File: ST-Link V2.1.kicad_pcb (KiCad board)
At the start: 2 copper layers, 46 parts, among them J1 Conn_01x08, J2 USB_OTG, J4 Conn_01x08, Q1 MMBT3904, U0 stm32, U1 MIC5219-3.3, X1 8MHz

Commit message: duh
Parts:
- C11, C12, C14, C15, C17, C5, C6, C7, C8, R10, R11, R12, R13, R14, R19, R20, R21, R22, R23, R26, R27, R29, R3, R30, R31, R4, R5, R6, R7, R8, R9: moved to F.Cu
- D1, D2, J2, U0: moved to B.Cu
- moved R2 69.0 mm to (126.2, 144.8), turned to 0 degrees
- moved C18 61.8 mm to (126.6, 139.8)
- moved R1 60.9 mm to (131.2, 139.7)
- moved LD2 54.8 mm to (130.2, 129.4)
- moved R9 51.8 mm to (140.9, 134.3)
- moved R10 51.6 mm to (135.6, 139.7)
- moved R11 50.5 mm to (130.6, 144.8)
- moved C11 50.4 mm to (136.9, 124.3)
- moved R14 50.4 mm to (135.0, 144.8)
- moved C14 50.3 mm to (143.5, 124.3)
- moved C12 49.5 mm to (140.2, 124.3), turned to 0 degrees
- moved Q1 48.5 mm to (131.1, 123.6)
- moved C7 46.6 mm to (129.0, 134.3)
- moved C6 45.2 mm to (139.8, 139.8)
- moved R27 41.0 mm to (144.0, 140.0)
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
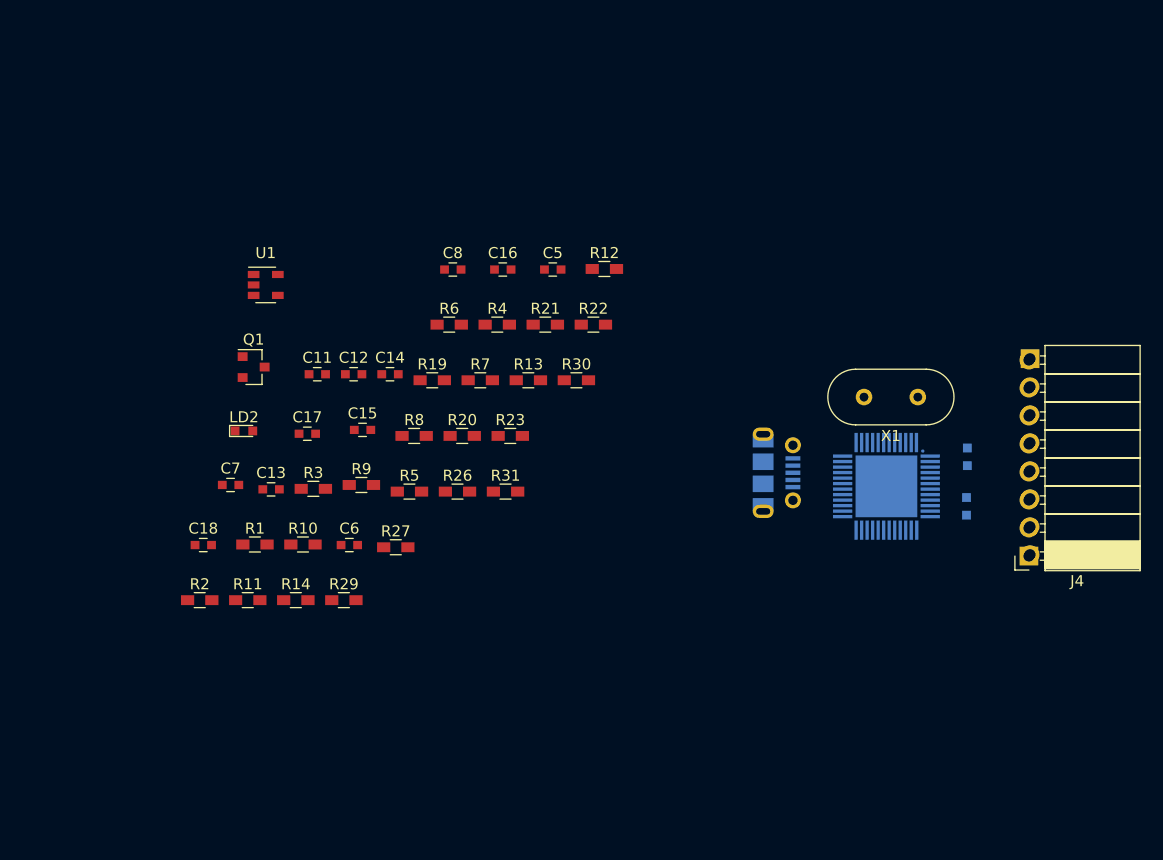
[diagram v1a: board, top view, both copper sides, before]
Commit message: ROUTE RESISTOR
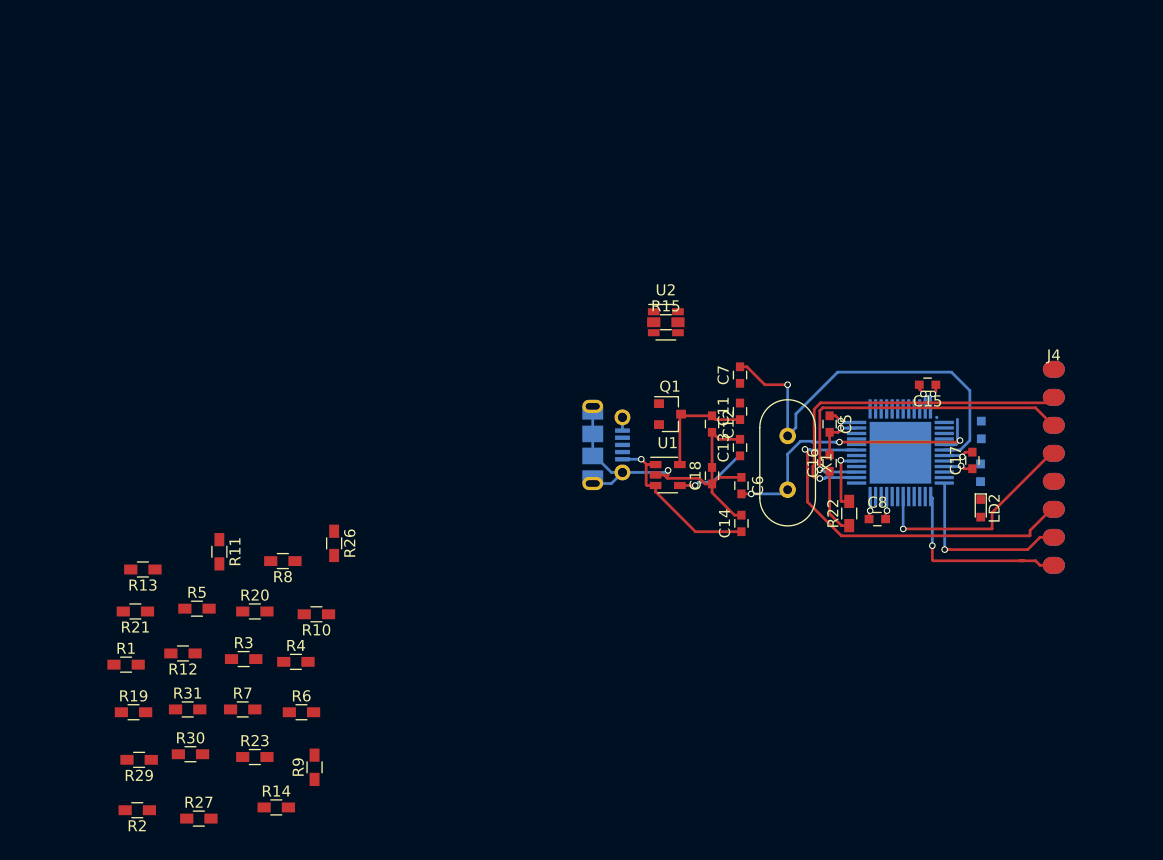
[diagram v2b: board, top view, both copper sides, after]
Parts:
- added R15: 4.7K, Resistors_SMD:R_0603_HandSoldering, F.Cu at (168.5, 119.5)
- added U2: USBLC6-2SC6, TO_SOT_Packages_SMD:SOT-23-6, F.Cu at (168.5, 119.5)
- J1, J4: footprint Socket_Strips:Socket_Strip_Angled_1x08_Pitch2.54mm -> MetalPad:METAL_PAD
- moved LD2 67.2 mm to (197.1, 136.4), turned to 270 degrees
- moved C17 60.4 mm to (196.3, 132.1), turned to 90 degrees
- moved R12 51.8 mm to (124.7, 149.6), turned to 180 degrees
- moved C15 51.4 mm to (192.3, 125.2), turned to 180 degrees
- moved R30 48.8 mm to (125.4, 158.8)
- moved C7 47.3 mm to (175.3, 124.3), turned to 90 degrees
- moved C18 46.6 mm to (172.7, 133.5), turned to 90 degrees
- moved R21 45.4 mm to (120.4, 145.8), turned to 180 degrees
- moved C8 44.7 mm to (187.7, 137.4)
- moved C13 42.7 mm to (175.3, 130.9), turned to 90 degrees
- moved R19 40.5 mm to (120.2, 154.9)
- moved U1 40.4 mm to (168.7, 133.4)
- moved R13 39.0 mm to (121.1, 142.0), turned to 180 degrees
- moved C11 38.5 mm to (175.3, 127.6), turned to 90 degrees
- moved Q1 38.0 mm to (168.9, 127.9)
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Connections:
- R7 pad 1: /USB_DP -> Net-(R15-Pad2)
- R8 pad 1: /USB_DM -> Net-(R8-Pad1)
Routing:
- net GNDREF: track 0.00 -> 50.3 mm, vias 0 -> 5
- net Net-(C7-Pad2): track 0.00 -> 37.2 mm, vias 0 -> 1
- net /T_SWO: track 0.00 -> 34.6 mm, vias 0 -> 1
- net /T_JTCK: track 0.00 -> 31.7 mm, vias 0 -> 1
- net /T_JTMS: track 0.00 -> 30.8 mm, vias 0 -> 1
- net Net-(C6-Pad2): track 0.00 -> 29.1 mm, vias 0 -> 3
- net /T_NRST: track 0.00 -> 20.3 mm, vias 0 -> 1
- net /3V3_ST_LINK: track 0.00 -> 20.1 mm, vias 0 -> 4
- net /STLINK_RX: track 0.00 -> 17.4 mm, vias 0 -> 1
- net /STLINK_TX: track 0.00 -> 16.6 mm, vias 0 -> 1
- net +5V: track 0.00 -> 16.6 mm, vias 0 -> 1
- net Net-(C13-Pad1): track 0.00 -> 6.44 mm, vias 0 -> 1
- net /MCO: track 0.00 -> 6.07 mm
- net Net-(R22-Pad2): track 0.00 -> 5.91 mm, vias 0 -> 1

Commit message: left abit
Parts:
- removed C12: 1uF, Capacitors_SMD:C_0603
- removed R1: 0, Resistors_SMD:R_0603_HandSoldering
- removed R15: 4.7K, Resistors_SMD:R_0603_HandSoldering
- removed R26: 10K, Resistors_SMD:R_0603_HandSoldering
- removed R27: [NA], Resistors_SMD:R_0603_HandSoldering
- added J3: Conn_01x06, Socket_Strips:Socket_Strip_Straight_1x06_Pitch2.54mm, F.Cu at (161.7, 95.1)
- C11, C13, C14, C15, C16, C17, C18, C5, C6, C7, C8, J4, Q1, R10, R11, R12, R13, R14, R19, R2, R20, R21, R23, R29, R3, R30, R31, R4, R5, R6, R7, R8, R9, U1, U2: moved to B.Cu
- D1, D2, J1, J2, U0: moved to F.Cu
- R22: value 100 -> 20; moved to B.Cu
- moved R2 76.1 mm to (167.2, 103.6), turned to 0 degrees
- moved R14 68.8 mm to (153.1, 97.7)
- moved R9 65.0 mm to (143.6, 95.3), turned to 270 degrees
- moved R19 64.7 mm to (155.5, 100.7), turned to 270 degrees
- moved R23 64.6 mm to (141.7, 95.3), turned to 90 degrees
- moved R3 64.1 mm to (167.5, 97.9)
- moved R12 62.3 mm to (162.3, 99.9), turned to 0 degrees
- moved R29 57.8 mm to (150.9, 109.9), turned to 270 degrees
- moved J1 57.7 mm to (170.9, 94.1)
- moved R13 56.2 mm to (159.2, 100.7), turned to 90 degrees
- moved R21 56.1 mm to (153.8, 100.7), turned to 90 degrees
- moved R30 55.9 mm to (152.6, 109.8), turned to 270 degrees
- moved R4 54.7 mm to (167.1, 106.2)
- moved R20 52.1 mm to (157.2, 100.7), turned to 270 degrees
- moved R11 51.6 mm to (162.3, 101.8), turned to 0 degrees
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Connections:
- net /RESET renamed /T_RESET
- net /ST_LINK_SWIM renamed /T_SWIM
- net /T_JTCK renamed /T_SWCLK_JTCK
- net /T_JTMS renamed /T_SWDIO_JTMS
- C11 pad 2: GNDREF -> GND
- C13 pad 2: GNDREF -> GND
- C14 pad 2: GNDREF -> GND
- C15 pad 2: GNDREF -> GND
- C16 pad 2: GNDREF -> GND
- C17 pad 2: GNDREF -> GND
- C18 pad 1: GNDREF -> /NRST
- C18 pad 2: GNDREF -> GND
- C5 pad 2: GNDREF -> GND
- C6 pad 1: GNDREF -> GND
- C7 pad 1: GNDREF -> GND
- C8 pad 2: GNDREF -> GND
- D1 pad 1: GNDREF -> GND
- J1 pad 1: GNDREF -> GND
- J1 pad 7: Net-(J1-Pad7) -> /MCO
- J2 pad 5: GNDREF -> GND
- J2 pad 6: GNDREF -> GND
- J4 pad 1: GNDREF -> GND
- LD2 pad 1: GNDREF -> GND
- R14 pad 2: GNDREF -> GND
- R23 pad 1: GNDREF -> GND
- R29 pad 2: GNDREF -> GND
- R31 pad 1: GNDREF -> /NRST
- R5 pad 1: GNDREF -> GND
- R7 pad 1: Net-(R15-Pad2) -> Net-(R7-Pad1)
- U0 pad 2: Net-(R26-Pad1) -> /PC13
- U0 pad 21: GNDREF -> GND
- U0 pad 23: GNDREF -> GND
- U0 pad 34: /STM_JTMS -> /STM_SWDIO_JTMS
- U0 pad 35: GNDREF -> GND
- U0 pad 37: /STM_JTCK -> /STM_SWCLK_JTCK
- U0 pad 47: GNDREF -> GND
- U0 pad 7: GNDREF -> /NRST
- U0 pad 8: GNDREF -> GND
- U1 pad 2: GNDREF -> GND
- U2 pad 1: Net-(R8-Pad1) -> Net-(R7-Pad1)
- U2 pad 2: GNDREF -> GND
- U2 pad 3: Net-(R15-Pad2) -> Net-(R8-Pad1)
- U2 pad 4: /USB_DP -> /USB_DM
- U2 pad 6: /USB_DM -> /USB_DP
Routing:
- net GND: track 0.00 -> 54.9 mm, vias 0 -> 2
- net GNDREF: track 50.3 -> 0.00 mm, vias 5 -> 0
- net Net-(C7-Pad2): track 37.2 -> 2.26 mm, vias 1 -> 0
- net /T_SWO: track 34.6 -> 0.00 mm, vias 1 -> 0
- net /T_SWCLK_JTCK: track 31.7 -> 0.00 mm, vias 1 -> 0
- net /3V3_ST_LINK: track 20.1 -> 51.3 mm, vias 4 -> 3
- net Net-(C6-Pad2): track 29.1 -> 2.26 mm, vias 3 -> 0
- net /T_NRST: track 20.3 -> 0.00 mm, vias 1 -> 0
- net /T_RESET: track 0.00 -> 19.0 mm, vias 0 -> 1
- net /STLINK_RX: track 17.4 -> 0.00 mm, vias 1 -> 0
- net Net-(Q1-Pad2): track 0.00 -> 17.0 mm, vias 0 -> 2
- net /STLINK_TX: track 16.6 -> 0.00 mm, vias 1 -> 0
- net /T_SWDIO_JTMS: track 30.8 -> 14.4 mm
- net /SWIM: track 0.00 -> 16.1 mm, vias 0 -> 1
- net Net-(J2-Pad3): track 0.00 -> 14.4 mm, vias 0 -> 1
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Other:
- net class Default: clearance 0.2 -> 0.199999
- rule trace_clearance: 0.2 -> 0.199999

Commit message: done routing
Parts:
- moved C16 9.32 mm to (161.4, 100.2), turned to 270 degrees
- moved R22 8.92 mm to (159.3, 100.7), turned to 270 degrees
- moved R12 6.97 mm to (157.6, 105.1), turned to 90 degrees
- moved C17 6.06 mm to (157.2, 100.2)
- moved R20 5.58 mm to (153.8, 105.1), turned to 90 degrees
- moved R13 5.56 mm to (155.7, 105.0), turned to 270 degrees
- moved C15 5.12 mm to (154.3, 109.3)
- moved C5 5.08 mm to (161.3, 104.9), turned to 270 degrees
- moved R11 4.35 mm to (159.4, 105.0), turned to 270 degrees
- moved R3 3.26 mm to (164.5, 99.3), turned to 270 degrees
- moved R4 2.94 mm to (164.5, 107.6), turned to 270 degrees
- moved LD2 2.72 mm to (164.5, 107.5)
- moved D2 2.69 mm to (164.5, 103.5)
- moved R2 2.63 mm to (164.5, 103.5), turned to 90 degrees
- moved D1 2.42 mm to (164.5, 99.3)
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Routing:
- net GND: track 54.9 -> 143.5 mm, vias 2 -> 16
- net /3V3_ST_LINK: track 51.3 -> 130.3 mm, vias 3 -> 11
- net /MCO: track 0.00 -> 35.6 mm, vias 0 -> 3
- net /PC13: track 0.00 -> 35.0 mm, vias 0 -> 6
- net /PWR_ENn: track 0.00 -> 32.3 mm, vias 0 -> 4
- net /USB_DP: track 0.00 -> 30.1 mm, vias 0 -> 1
- net /USB_DM: track 0.00 -> 28.2 mm, vias 0 -> 1
- net /NRST: track 6.68 -> 29.9 mm, vias 1 -> 2
- net /STLINK_TX: track 0.00 -> 16.7 mm, vias 0 -> 1
- net /T_SWO: track 0.00 -> 15.3 mm, vias 0 -> 1
- net /LED_STLINK: track 0.00 -> 15.0 mm, vias 0 -> 3
- net /T_NRST: track 0.00 -> 14.8 mm, vias 0 -> 3
- net /STLINK_RX: track 0.00 -> 14.0 mm, vias 0 -> 1
- net /T_SWCLK_JTCK: track 0.00 -> 12.4 mm, vias 0 -> 1
- net /STM_SWDIO_JTMS: track 0.00 -> 12.2 mm, vias 0 -> 1
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
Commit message: working footprint(need to reroute)
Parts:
- removed the J1 at (168.7, 94.6)
- added J3: Conn_01x08, MetalPad:METAL_PAD, F.Cu at (168.7, 94.6)
- moved R4 0.18 mm to (138.7, 112.1)
- moved R6 0.10 mm to (138.7, 110.1)
- moved R11 0.09 mm to (145.4, 95.3)
- moved J4 0.05 mm to (168.7, 94.6)
- moved R9 0.05 mm to (141.7, 95.3)
- renumbered C18 to C1, C13 to C10, C7 to C2, C6 to C3, C15 to C4, C17 to C5, C8 to C6, C16 to C7, C5 to C8, C14 to C9, J2 to J1, J3 to J2, LD2 to LD1, R31 to R1, R14 to R10, R10 to R11, R3 to R12, R2 to R13, R11 to R14, R22 to R15, R4 to R16, R20 to R17, R21 to R18, R12 to R19, R29 to R2, R13 to R20, R19 to R21, R30 to R3, R7 to R4, R8 to R5, R5 to R7, R9 to R8, R23 to R9, U2 to U1, U0 to U2, U1 to U3
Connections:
- D2 pad 2: Net-(D2-Pad2) -> /3V3_ST_LINK
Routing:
- net /3V3_ST_LINK: track 130.3 -> 133.1 mm, vias 11 -> 13
- added copper zone on F.Cu, net /3V3_ST_LINK
- added copper zone on B.Cu, net GND
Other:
- board outline added: 37.4 x 21.3 mm

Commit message: routing
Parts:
- removed LD1: LED,RED, LEDs:LED_0603
- added D3: LED, LEDs:LED_0603, B.Cu at (147.1, 112.3)
- C4, C5, C6, C8: footprint Capacitors_SMD:C_0603 -> Capacitors_SMD:C_0805
- D1, D2: moved to B.Cu
- R1, R10, R11, R14, R15, R16, R19, R2, R20, R21, R3, R4, R5, R6, R7, R8, R9: footprint Resistors_SMD:R_0603_HandSoldering -> Resistors_SMD:R_0603
- R12, R13, R17, R18: footprint Resistors_SMD:R_0603_HandSoldering -> Resistors_SMD:R_0805
- moved C5 20.1 mm to (138.0, 106.2), turned to 270 degrees
- moved Q1 20.0 mm to (119.6, 101.4)
- moved R9 19.4 mm to (122.9, 100.3)
- moved C7 19.4 mm to (142.9, 106.2), turned to 90 degrees
- moved C8 19.3 mm to (142.6, 109.8)
- moved R3 19.3 mm to (134.0, 115.0)
- moved R14 19.2 mm to (140.8, 109.8)
- moved R19 19.1 mm to (139.1, 109.8)
- moved C9 19.0 mm to (126.7, 102.7)
- moved C10 19.0 mm to (126.7, 104.3), turned to 0 degrees
- moved C6 19.0 mm to (133.6, 109.8)
- moved R10 18.9 mm to (134.8, 102.5)
- moved C11 18.9 mm to (130.8, 109.5)
- moved R8 18.9 mm to (125.4, 100.3)
- moved R20 18.8 mm to (137.4, 109.8)
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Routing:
- net GND: track 143.6 -> 0.00 mm, vias 16 -> 0
- net /3V3_ST_LINK: track 133.1 -> 0.00 mm, vias 13 -> 0
- net /MCO: track 35.4 -> 0.00 mm, vias 3 -> 0
- net /PC13: track 35.0 -> 0.00 mm, vias 6 -> 0
- net /PWR_ENn: track 32.6 -> 0.00 mm, vias 4 -> 0
- net /USB_DP: track 30.1 -> 0.00 mm, vias 1 -> 0
- net /NRST: track 29.9 -> 0.00 mm, vias 2 -> 0
- net /USB_DM: track 28.2 -> 0.00 mm, vias 1 -> 0
- net /T_RESET: track 19.1 -> 0.00 mm, vias 1 -> 0
- net /T_SWIM: track 18.7 -> 0.00 mm, vias 1 -> 0
- net /STLINK_TX: track 16.7 -> 0.00 mm, vias 1 -> 0
- net /T_SWO: track 15.3 -> 0.00 mm, vias 1 -> 0
- net /LED_STLINK: track 15.0 -> 0.00 mm, vias 3 -> 0
- net /T_NRST: track 14.8 -> 0.00 mm, vias 3 -> 0
- net /STLINK_RX: track 14.0 -> 0.00 mm, vias 1 -> 0
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- removed copper zone on F.Cu, net /3V3_ST_LINK
- removed copper zone on B.Cu, net GND
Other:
- board size 37.4 x 21.3 mm -> 46 x 20.6 mm

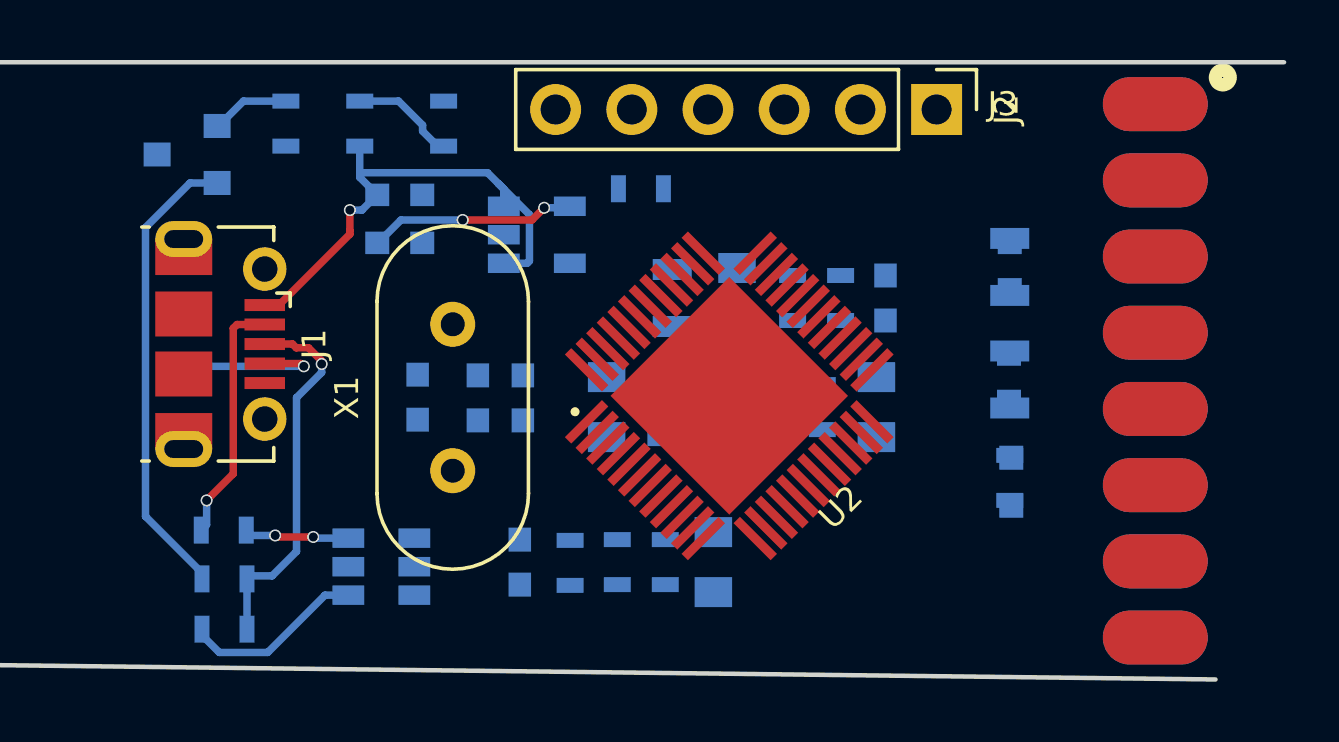
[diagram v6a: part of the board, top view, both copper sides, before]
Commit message: left 3v3 and gnd
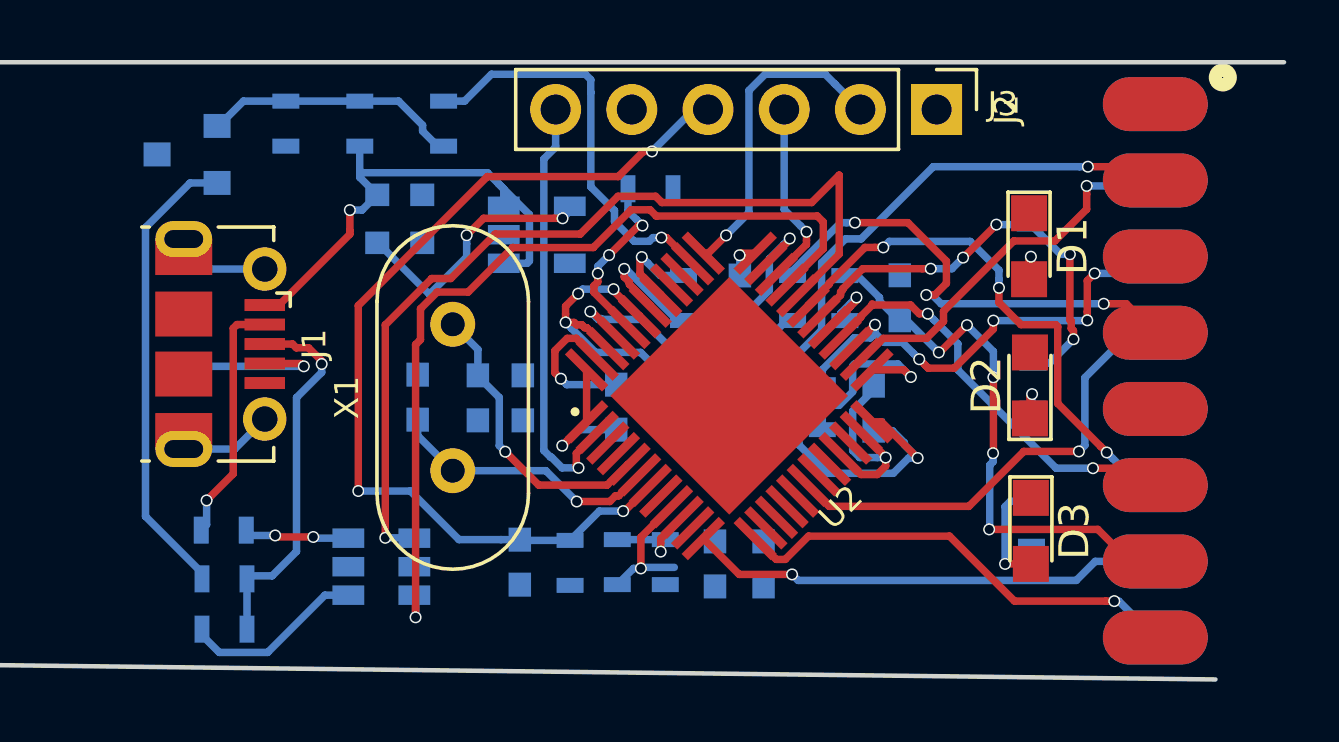
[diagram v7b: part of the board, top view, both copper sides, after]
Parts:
- added C12: 100nF, Capacitors_SMD:C_0603, B.Cu at (138.9, 115.0)
- C10, C9: value 1uF -> 22nF
- C11: value 1uF -> 10uF
- C4, C5, C6, C8: footprint Capacitors_SMD:C_0805 -> Capacitors_SMD:C_0603
- D1, D2, D3: footprint LEDs:LED_0603 -> LEDs:LED_0805; moved to F.Cu
- R12, R13: value 220 -> 510; footprint Resistors_SMD:R_0805 -> Resistors_SMD:R_0603
- R16: value 1K -> 510
- R17, R18: footprint Resistors_SMD:R_0805 -> Resistors_SMD:R_0603
- R6: value 1K5 -> 4K7
- moved C6 8.90 mm to (142.5, 109.8)
- moved C8 7.50 mm to (137.2, 115.0), turned to 90 degrees
- moved C4 6.10 mm to (133.9, 109.8), turned to 90 degrees
- moved D3 1.76 mm to (147.8, 113.9)
- moved R16 1.69 mm to (147.8, 113.7), turned to 270 degrees
- moved R12 0.96 mm to (147.8, 104.4), turned to 90 degrees
- moved D1 0.92 mm to (147.7, 104.4), turned to 270 degrees
- moved R13 0.80 mm to (147.8, 109.1)
- moved D2 0.74 mm to (147.7, 109.1)
- moved C7 0.47 mm to (143.4, 106.2)
- moved R18 0.38 mm to (136.2, 106.2)
- moved R10 0.32 mm to (135.1, 102.5)
- moved R15 0.14 mm to (141.6, 106.2)
- moved C5 0.10 mm to (138.1, 106.2)
- moved R17 0.05 mm to (135.7, 109.8)
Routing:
- net /NRST: track 0.00 -> 31.7 mm, vias 0 -> 3
- net /USB_DM: track 0.00 -> 30.0 mm, vias 0 -> 1
- net /USB_DP: track 0.00 -> 28.7 mm, vias 0 -> 1
- net GND: track 0.00 -> 23.2 mm, vias 0 -> 3
- net /3V3_ST_LINK: track 0.00 -> 22.9 mm, vias 0 -> 4
- net /T_SWIM: track 0.00 -> 19.0 mm, vias 0 -> 1
- net /MCO: track 0.00 -> 18.8 mm, vias 0 -> 5
- net /T_SWO: track 0.00 -> 18.0 mm, vias 0 -> 3
- net /T_SWDIO_JTMS: track 0.00 -> 16.5 mm, vias 0 -> 5
- net /T_RESET: track 0.00 -> 16.2 mm, vias 0 -> 3
- net /STLINK_TX: track 0.00 -> 15.9 mm, vias 0 -> 1
- net /T_NRST: track 0.00 -> 15.6 mm, vias 0 -> 1
- net /STLINK_RX: track 0.00 -> 15.3 mm, vias 0 -> 1
- net /LED_STLINK: track 0.00 -> 14.7 mm, vias 0 -> 5
- net /PC13: track 0.00 -> 14.4 mm, vias 0 -> 1
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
